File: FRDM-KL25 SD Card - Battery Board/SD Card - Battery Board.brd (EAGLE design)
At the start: 81.3 x 53.3 mm, 64 parts, among them J3 SSW-108-02-S-D, J4 SSW-110-02-S-D, J5 SSW-108-02-S-D, J6 SSW-106-02-S-D, U1 TPS63001, U2 TPS63002, U3 BQ27510DRZT-G3, U4 BQ24210DQCT

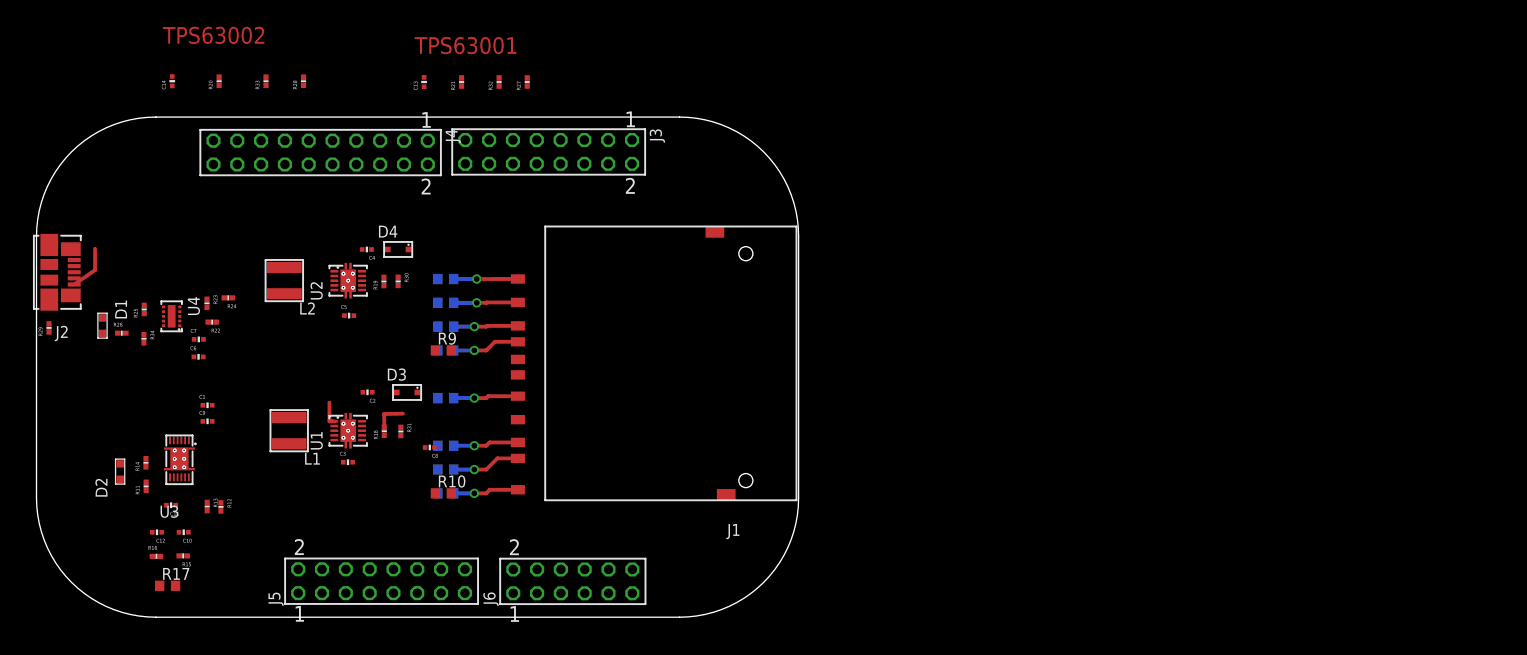
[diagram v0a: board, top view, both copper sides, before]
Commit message: FRDM-KL26Z: Added 5V+ and changed VCC to 3V3+, moved battery section off PCB in preperation for branch
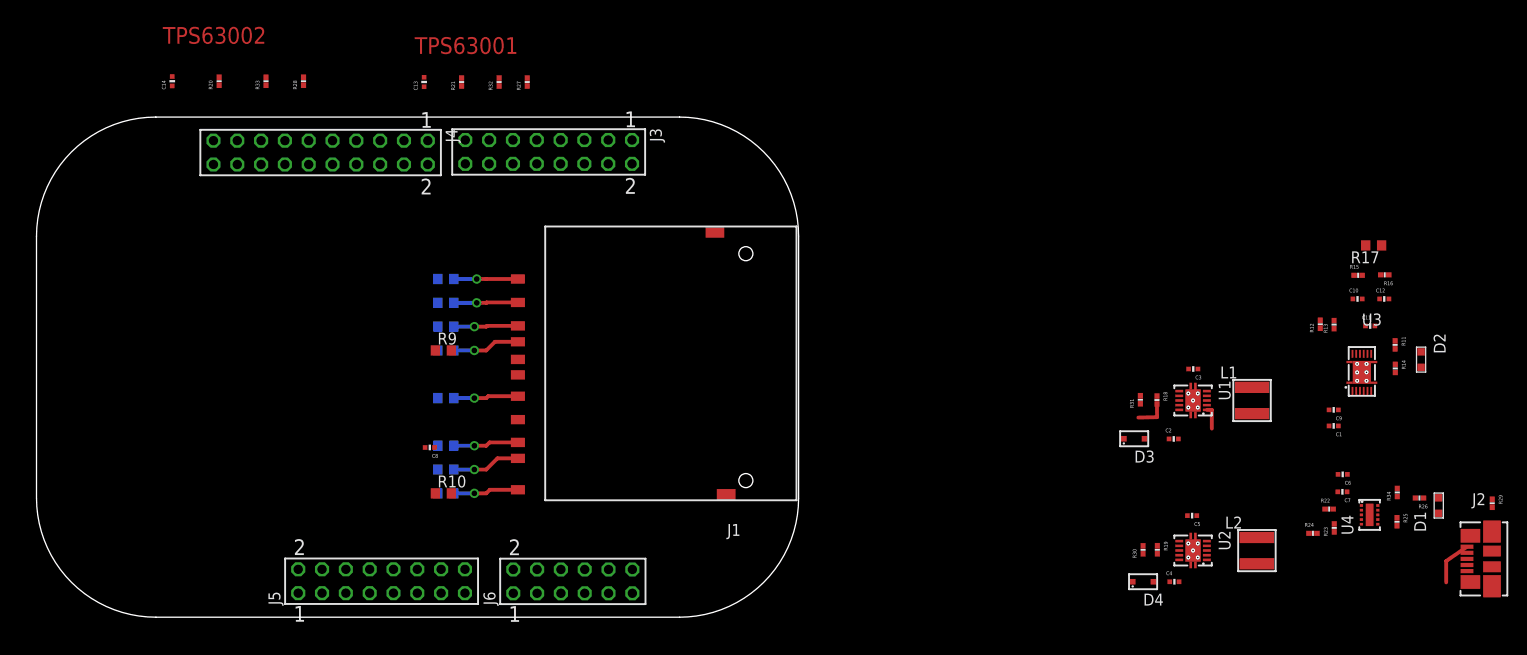
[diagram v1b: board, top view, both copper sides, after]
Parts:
- moved R29 155.1 mm to (140.3, 9.33), turned to 270 degrees
- moved J2 151.7 mm to (137.6, 3.40), turned to 180 degrees
- moved D1 143.8 mm to (134.6, 9.09), turned to 270 degrees
- moved R26 139.5 mm to (132.5, 9.89), turned to 180 degrees
- moved D2 139.3 mm to (132.7, 24.7), turned to 90 degrees
- moved R25 135.5 mm to (130.2, 7.36), turned to 270 degrees
- moved R34 134.7 mm to (130.2, 10.5), turned to 90 degrees
- moved R16 134.4 mm to (128.9, 33.7), turned to 180 degrees
- moved R11 134.1 mm to (130.0, 26.2), turned to 270 degrees
- moved R17 133.7 mm to (127.7, 36.8), turned to 180 degrees
- moved R14 133.6 mm to (130.0, 23.7), turned to 270 degrees
- moved C12 133.2 mm to (128.8, 31.1), turned to 0 degrees
- moved U4 129.5 mm to (127.2, 8.09), turned to 270 degrees
- moved C11 129.3 mm to (127.3, 28.2), turned to 0 degrees
- moved R15 128.8 mm to (126.0, 33.6), turned to 0 degrees
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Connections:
- net N$2 renamed +5V
- net VCC renamed +3V3

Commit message: FRDM-KL25Z: Corrected J3, J4, J5 and J6 connections on the schematic. Jumpers where added for 3V3, 5V and TPS63001 EN and BQ24210 EN. SPI Connections have been labled to enable SD card to connect to PD1, PD2 and PD3. Layed out and connected TPS63002 circuit as well as BQ42410 circuit.
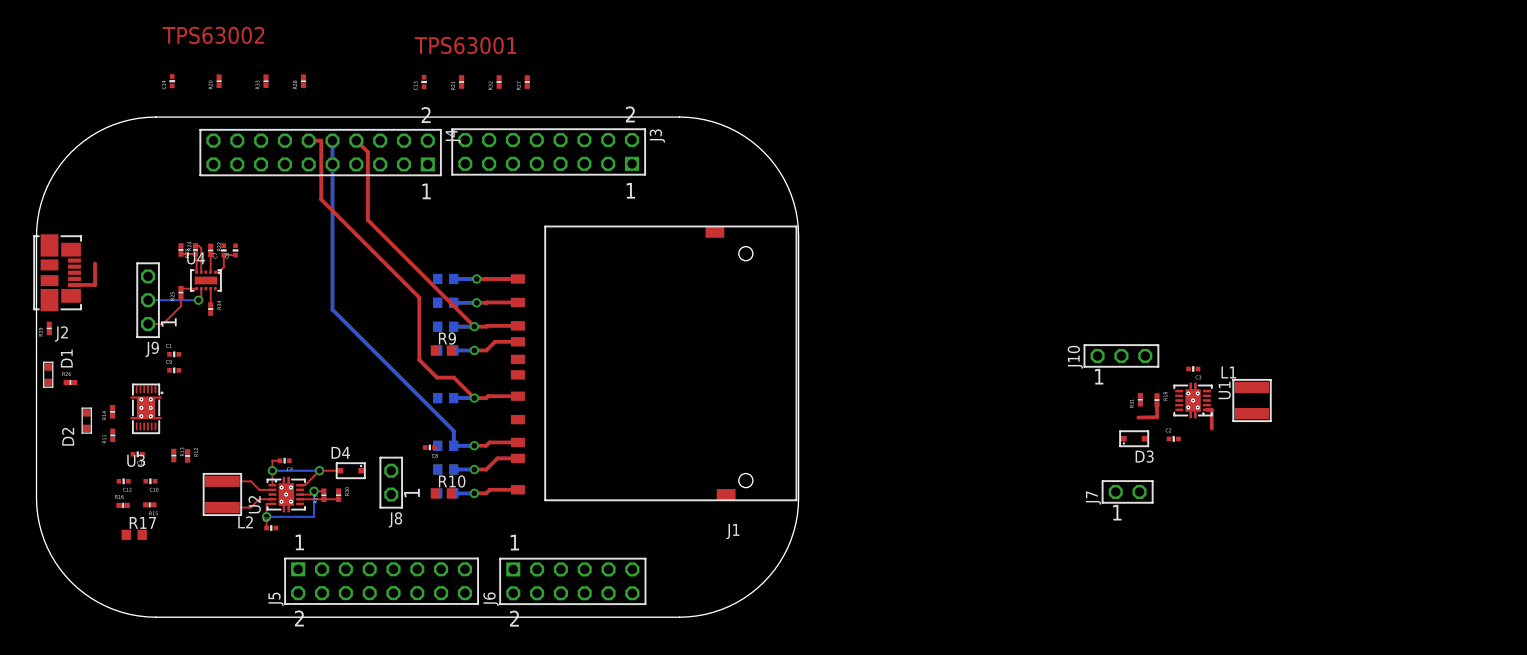
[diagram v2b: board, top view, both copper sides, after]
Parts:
- added J10, J9: SSW-103-02-S-S, Kas-Connectors:SSW-103-02-S-S
- added J7, J8: SSW-102-02-S-S, Kas-Connectors:SSW-102-02-S-S
- moved R29 155.0 mm to (-13.6, 28.0), turned to 90 degrees
- moved J2 151.6 mm to (-10.9, 33.9), turned to 0 degrees
- moved D1 149.0 mm to (-13.7, 23.0), turned to 90 degrees
- moved R26 144.4 mm to (-11.3, 22.2), turned to 0 degrees
- moved D2 142.5 mm to (-9.58, 18.1), turned to 270 degrees
- moved R11 137.1 mm to (-6.81, 16.6), turned to 90 degrees
- moved R14 136.9 mm to (-6.83, 19.1), turned to 90 degrees
- moved R16 136.8 mm to (-5.71, 9.11), turned to 0 degrees
- moved C12 135.8 mm to (-5.65, 11.7), turned to 180 degrees
- moved R17 135.7 mm to (-4.52, 5.97), turned to 0 degrees
- moved C11 132.2 mm to (-4.15, 14.6), turned to 180 degrees
- moved R25 132.0 mm to (0.46, 31.8), turned to 90 degrees
- moved R15 131.2 mm to (-2.86, 9.16), turned to 180 degrees
- moved C10 130.2 mm to (-2.80, 11.7), turned to 180 degrees
- moved U3 129.7 mm to (-3.26, 19.5), turned to 180 degrees
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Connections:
- removed net 3.3V_KL25Z--ADD-JUMPER: D3.P$1
- removed net 5V_KL25Z--ADD-JUMPER: D4.P$1
- removed net SOI-MISO-0.0: J4.12
- removed net SPI-MISO: J1.P$7, R5.1
- removed net SPI-MOSI: J1.P$2, R3.1
- removed net SPI-MOSI-0.0: J4.14
- removed net SPI-SCK-0.0: J4.10
- removed net SPI-SCK-0.1: J3.8
- removed net SPI-SCLK: J1.P$5, R4.1
- removed net VIN: J5.16
- new net 3.3V_KL25Z: D3.P$1, J7.2
- new net 3V3+: J7.1
- new net 5V_KL25Z: D4.P$1, J8.2
- new net N$2: J10.2, U1.P$6
- new net SELF_EN: J9.1, R25.1
- new net SPI-MISO-SD: J1.P$7, J4.10, R5.1
- new net SPI-MOSI-SD: J1.P$2, J4.8, R3.1
- new net SPI-SCLK-0.1: J3.9
- new net SPI-SCLK-SD: J1.P$5, J4.12, R4.1
- new net UC_3V3_EN: J10.1
- new net UC_EN_CHARGE: J9.3
- new net VCC: C4.2, D4.P$2, U2.P$1, U2.P$10
- net !BAT_LOW: now also J10.3; no longer U1.P$6
- net !FN: now also J9.2; no longer R25.1
- net +5V: now also J5.16, J8.1; no longer C4.2, D4.P$2, U2.P$1, U2.P$10
- net GND: now also J4.14; no longer J4.8
- net I2C-SCL-0: now also J3.14; no longer J3.3
- net I2C-SCL-1.0: now also J4.20; no longer J4.2
- net I2C-SCL-1.1: now also J3.13; no longer J3.4
- net I2C-SCL-1.2: now also J6.12; no longer J6.11
- net I2C-SDA-0: now also J3.16; no longer J3.1
- net I2C-SDA-1.0: now also J4.18; no longer J4.4
- net I2C-SDA-1.1: now also J3.15; no longer J3.2
- net I2C-SDA-1.2: now also J6.10; no longer J6.9
- net INT1-21002: now also J3.12; no longer J3.5
- net INT1-8700: now also J3.6; no longer J3.11
- net INT2-21002: now also J4.2; no longer J4.20
- net INT2-8700: now also J3.10; no longer J3.7
- net SPI-CSB-21002: now also J4.6; no longer J4.16
- net SPI-CSB-8700: now also J6.6; no longer J6.5
- net SPI-MISO-0.1: now also J3.1; no longer J3.16
- net SPI-MOSI-0.1: now also J3.11; no longer J3.6
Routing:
- net SPI-MISO-SD: track 0.00 -> 44.9 mm, vias 0 -> 1
- net SPI-SCLK-SD: track 0.00 -> 43.5 mm, vias 0 -> 1
- net SPI-MOSI-SD: track 0.00 -> 31.9 mm, vias 0 -> 1
- net PACK+: track 3.41 -> 17.1 mm, vias 0 -> 2
- net VCC: track 0.00 -> 13.4 mm, vias 0 -> 2
- net SPI-MISO: track 6.99 -> 0.00 mm, vias 1 -> 0
- net SPI-SCLK: track 6.93 -> 0.00 mm, vias 1 -> 0
- net SPI-MOSI: track 6.88 -> 0.00 mm, vias 1 -> 0
- net !FN: track 0.00 -> 6.74 mm, vias 0 -> 1
- net N$14: track 0.00 -> 5.71 mm
- net N$15: track 0.00 -> 5.70 mm
- net SELF_EN: track 0.00 -> 5.32 mm
- net PS/SYNC-2: track 0.00 -> 4.11 mm
- net +5V_CHARGE: track 0.00 -> 3.67 mm
- net N$33: track 0.00 -> 3.55 mm
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
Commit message: FRDM-KL25Z: Connected all major ICs to their respective components ad moved them into a resanable location. I2C connections were made as were the 3V3 and 5V connctions to the main board. It was decided to leave VIN unconnected as this in reality will not be needed as a 3V3 rail is avaiable from the battery. Headers were added to allow for connecting and disconnecting the 3V3 and 5V rails as well as selecting how to enable/disable the buck/boost ICs. Headers were also added to allow the choosing of I2C-0 or I2C-1. Also added was the ability to pull the I2C to 3V3 or if provided by another board in the stack to do so there instead.
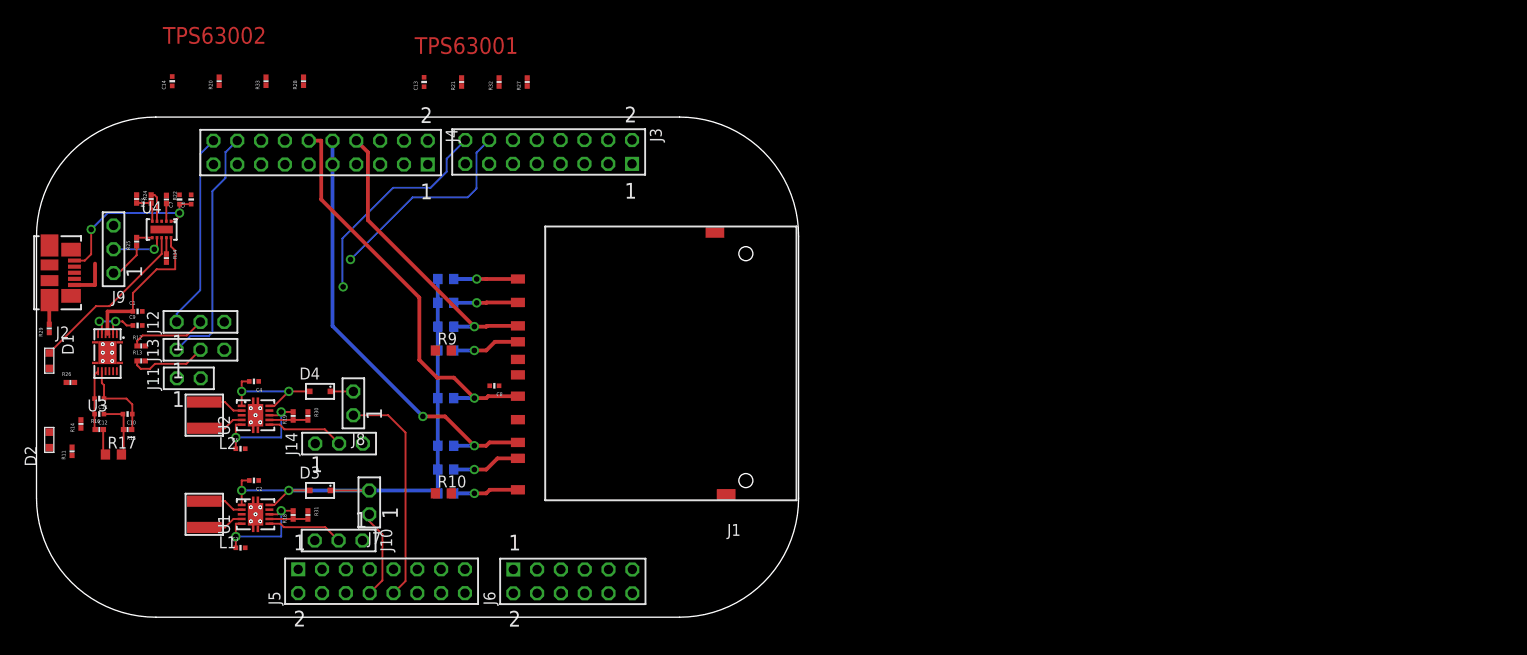
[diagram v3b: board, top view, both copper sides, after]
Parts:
- added J11: SSW-102-02-S-S, Kas-Connectors:SSW-102-02-S-S
- added J12, J13, J14: SSW-103-02-S-S, Kas-Connectors:SSW-103-02-S-S
- moved L1 112.4 mm to (2.95, 8.15), turned to 0 degrees
- moved C3 103.4 mm to (6.81, 4.59), turned to 0 degrees
- moved U1 100.7 mm to (8.41, 8.15), turned to 270 degrees
- moved C2 98.2 mm to (8.24, 11.8), turned to 180 degrees
- moved R18 92.9 mm to (12.4, 8.08), turned to 90 degrees
- moved R31 89.6 mm to (14.0, 8.08), turned to 270 degrees
- moved D3 87.0 mm to (15.3, 10.7), turned to 180 degrees
- moved J10 85.8 mm to (17.3, 5.36), turned to 180 degrees
- moved J7 80.9 mm to (20.5, 9.42), turned to 90 degrees
- moved R12 12.7 mm to (-3.78, 26.1), turned to 0 degrees
- moved R13 10.7 mm to (-3.78, 24.5), turned to 0 degrees
- moved C8 9.52 mm to (33.9, 21.9)
- moved J8 9.37 mm to (18.8, 20.0)
- moved C5 9.07 mm to (6.81, 15.2)
- moved D4 9.07 mm to (15.3, 21.3)
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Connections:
- net VCC renamed N$20
- removed net +5V: J5.16, J8.1
- removed net 3.3V++: J5.4, J5.8
- removed net 3V3+: J7.1
- removed net 5V++: J5.10
- new net N$13: J14.2, U2.P$6
- new net N$17: D3.P$1, J7.2
- new net N$18: D4.P$1, J8.2
- new net N$4: J11.1, R12.2, R13.2
- new net UC_5V_EN: J14.3
- new net VIN: J5.16
- net !BAT_LOW: now also J14.1; no longer U2.P$6
- net +3V3: now also J11.2; no longer R12.2, R13.2
- net 3.3V_KL25Z: now also J5.4, J5.8, J7.1; no longer D3.P$1, J7.2
- net 5V_KL25Z: now also J5.10, J8.1; no longer D4.P$1, J8.2
- net I2C-SCL-0: now also J12.3
- net I2C-SCL-1.0: now also J12.1
- net I2C-SDA-0: now also J13.3
- net I2C-SDA-1.0: now also J13.1
- net SCL: now also J12.2
- net SDA: now also J13.2
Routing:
- net +3V3: track 2.53 -> 52.4 mm, vias 0 -> 2
- net PACK+: track 17.1 -> 43.6 mm, vias 2 -> 4
- net I2C-SDA-1.0: track 0.00 -> 26.2 mm
- net 5V_KL25Z: track 0.00 -> 24.0 mm
- net I2C-SDA-0: track 0.00 -> 23.5 mm, vias 0 -> 1
- net I2C-SCL-0: track 0.00 -> 22.3 mm, vias 0 -> 1
- net I2C-SCL-1.0: track 0.00 -> 21.0 mm
- net !CHARGE: track 0.00 -> 18.1 mm
- net +5V_CHARGE: track 3.67 -> 18.5 mm, vias 0 -> 2
- net 3.3V_KL25Z: track 0.00 -> 9.55 mm
- net N$7: track 0.00 -> 9.06 mm
- net N$13: track 0.00 -> 8.27 mm
- net SDA: track 0.00 -> 8.21 mm
- net SCL: track 0.00 -> 8.13 mm
- net N$2: track 0.00 -> 8.13 mm
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
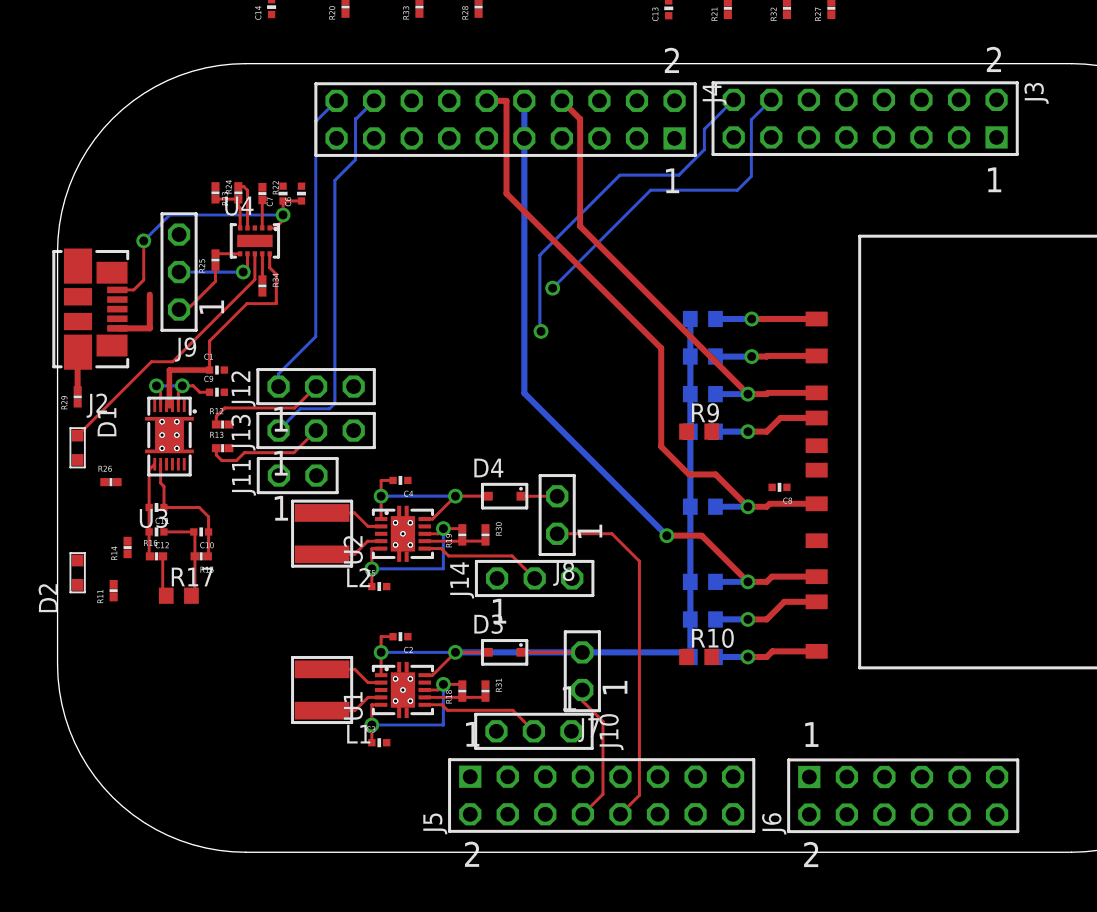
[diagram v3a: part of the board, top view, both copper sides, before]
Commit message: FRDM-KL25Z: Most of the board is now connected, routed lines need to be cleaned up but there appears to be some difficulty in doing this. There will be an attempt to do the board inverted and this will carry on on a branch I for inverted (doing everything on teh bottom of teh board. At this point all DRC issues have been cleared or ignored as non issues
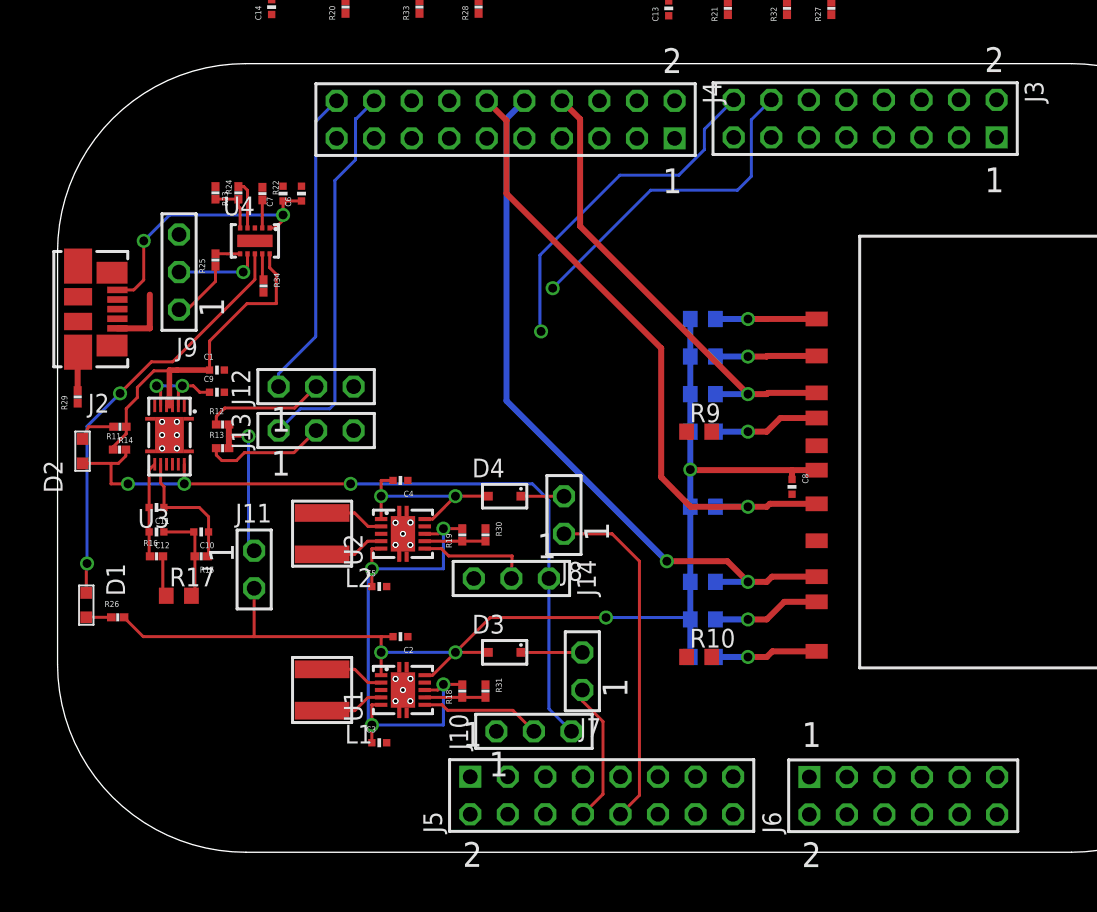
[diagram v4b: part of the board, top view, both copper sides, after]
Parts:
- moved D1 10.7 mm to (-13.0, 13.9)
- moved R11 9.55 mm to (-10.8, 24.4), turned to 0 degrees
- moved R26 9.16 mm to (-10.9, 13.1)
- moved D2 8.23 mm to (-13.3, 24.3)
- moved R14 8.19 mm to (-10.7, 26.0), turned to 180 degrees
- moved J11 7.00 mm to (-1.65, 16.3), turned to 270 degrees
- moved J14 1.57 mm to (15.7, 15.7), turned to 180 degrees
- moved C8 0.85 mm to (34.7, 21.9), turned to 270 degrees
- moved J8 0.46 mm to (19.3, 20.0)
- moved R34 0.08 mm to (-1.02, 35.5)
- turned J10 to 0 degrees
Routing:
- net !BAT_LOW: track 0.00 -> 52.6 mm, vias 0 -> 3
- net +3V3: track 52.4 -> 83.9 mm, vias 2 -> 4
- net PACK+: track 43.6 -> 62.4 mm
- net N$4: track 0.00 -> 10.8 mm, vias 0 -> 1
- net !CHARGE: track 18.1 -> 28.5 mm, vias 0 -> 2
- net N$5: track 0.00 -> 2.62 mm
- net SPI-MISO-SD: track 47.2 -> 49.2 mm
- net N$10: track 0.00 -> 1.70 mm
- net N$13: track 8.27 -> 7.64 mm
